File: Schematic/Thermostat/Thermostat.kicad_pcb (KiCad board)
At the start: 2 copper layers, 50 x 50 mm, 28 parts, among them J1 Heater, J2 230VAC IN, U1 TS321ILT

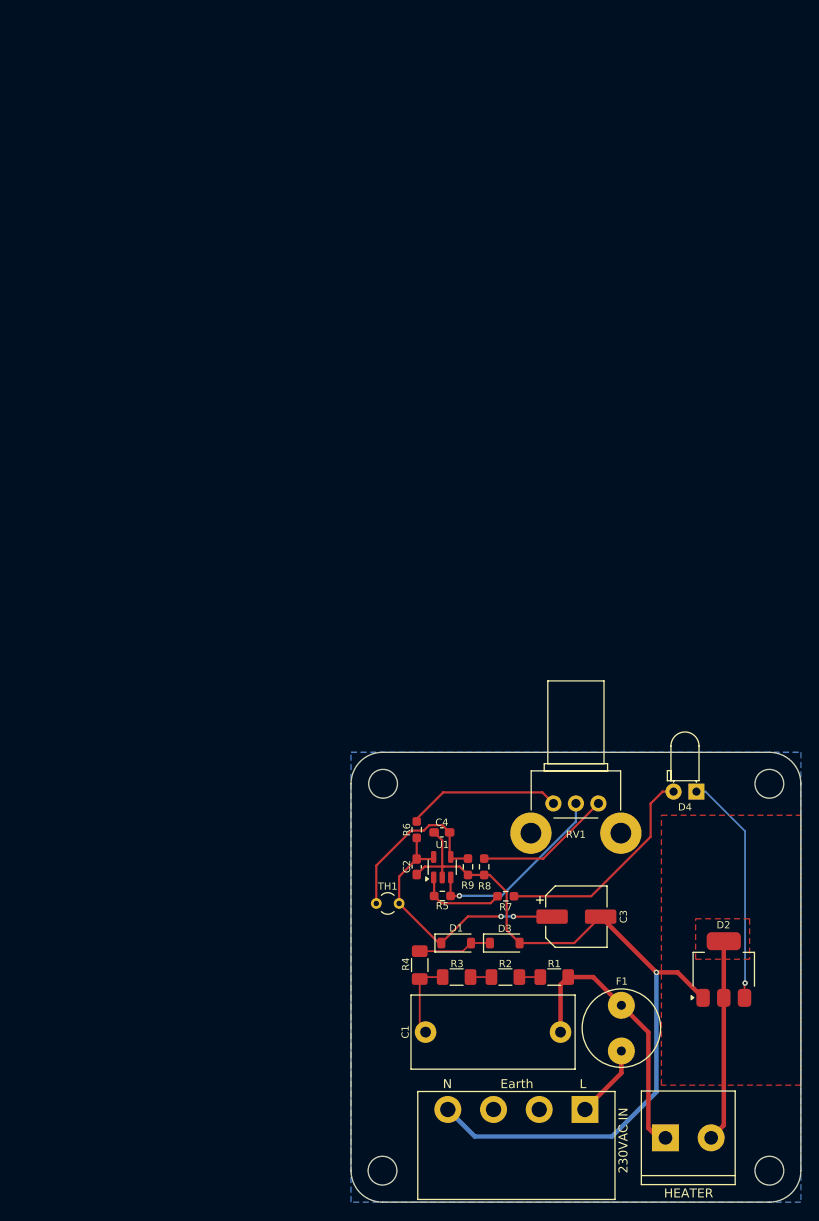
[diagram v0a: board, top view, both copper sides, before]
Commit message: Rearranged schematic, added copy ring
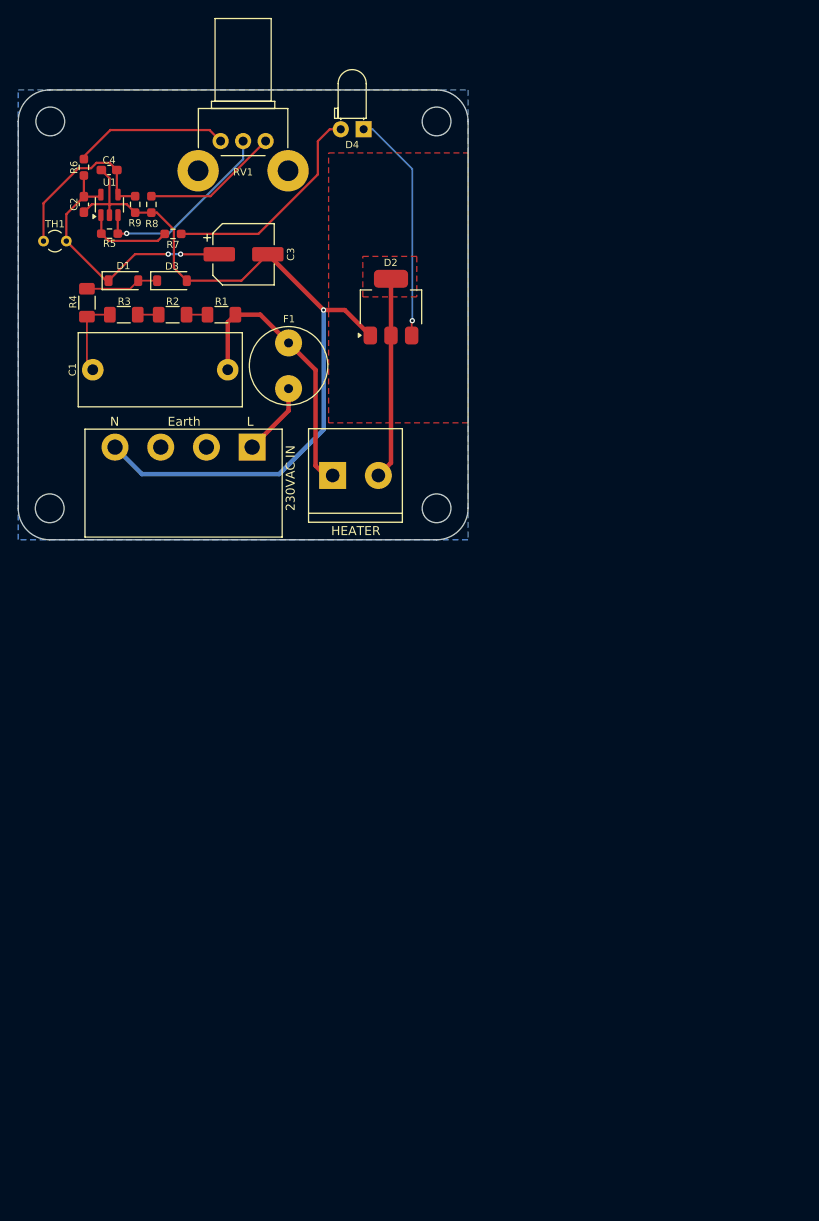
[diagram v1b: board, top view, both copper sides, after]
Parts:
- moved C1 82.4 mm to (35.3, 61.5)
- moved C2 82.4 mm to (34.3, 43.1)
- moved C4 82.4 mm to (37.1, 39.3)
- moved D1 82.4 mm to (38.7, 51.6)
- moved D2 82.4 mm to (68.4, 54.5)
- moved D3 82.4 mm to (44.1, 51.6)
- moved D4 82.4 mm to (65.4, 34.8)
- moved G*** 82.4 mm to (52.0, 49.4)
- moved H1 82.4 mm to (30.5, 76.9)
- moved H2 82.4 mm to (73.5, 76.9)
- moved H3 82.4 mm to (30.6, 33.9)
- moved H4 82.4 mm to (73.5, 33.9)
- moved R4 82.4 mm to (34.6, 54.0)
- moved R5 82.4 mm to (37.2, 46.4)
- moved R6 82.4 mm to (34.3, 39.0)
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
